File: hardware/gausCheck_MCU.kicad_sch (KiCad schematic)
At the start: 17 parts, among them J2 SWD, SW1 PTS810, U3 ATSAML22N18A-AUT, Y1 32.768kHz

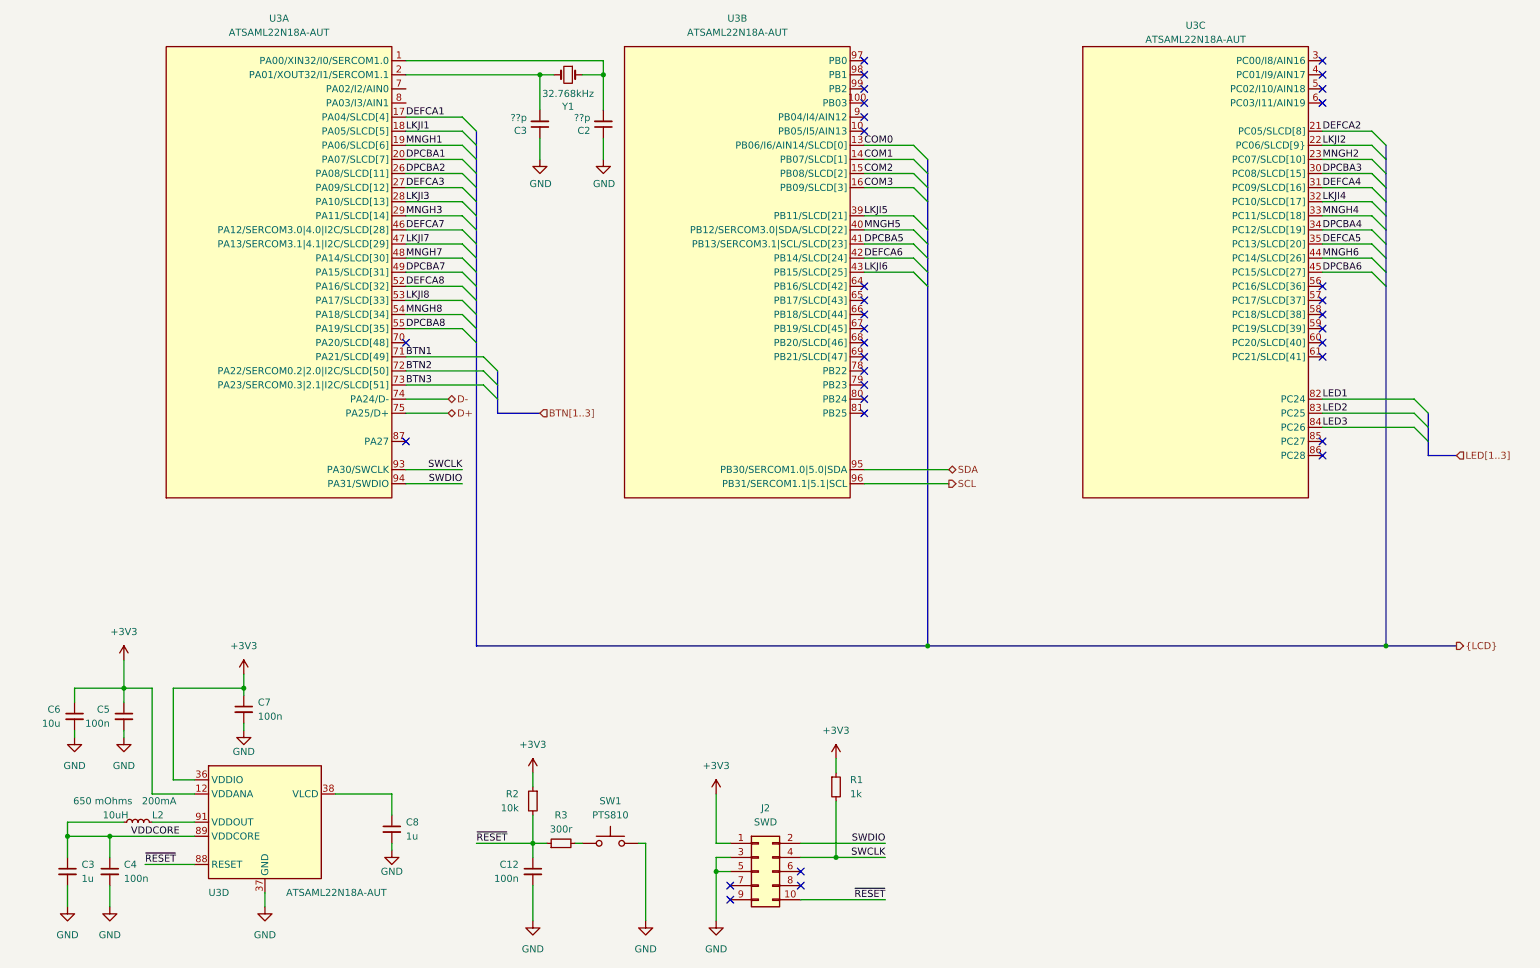
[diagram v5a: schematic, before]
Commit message: moved buttons to the side JTAG to the bottom reset to the bottom
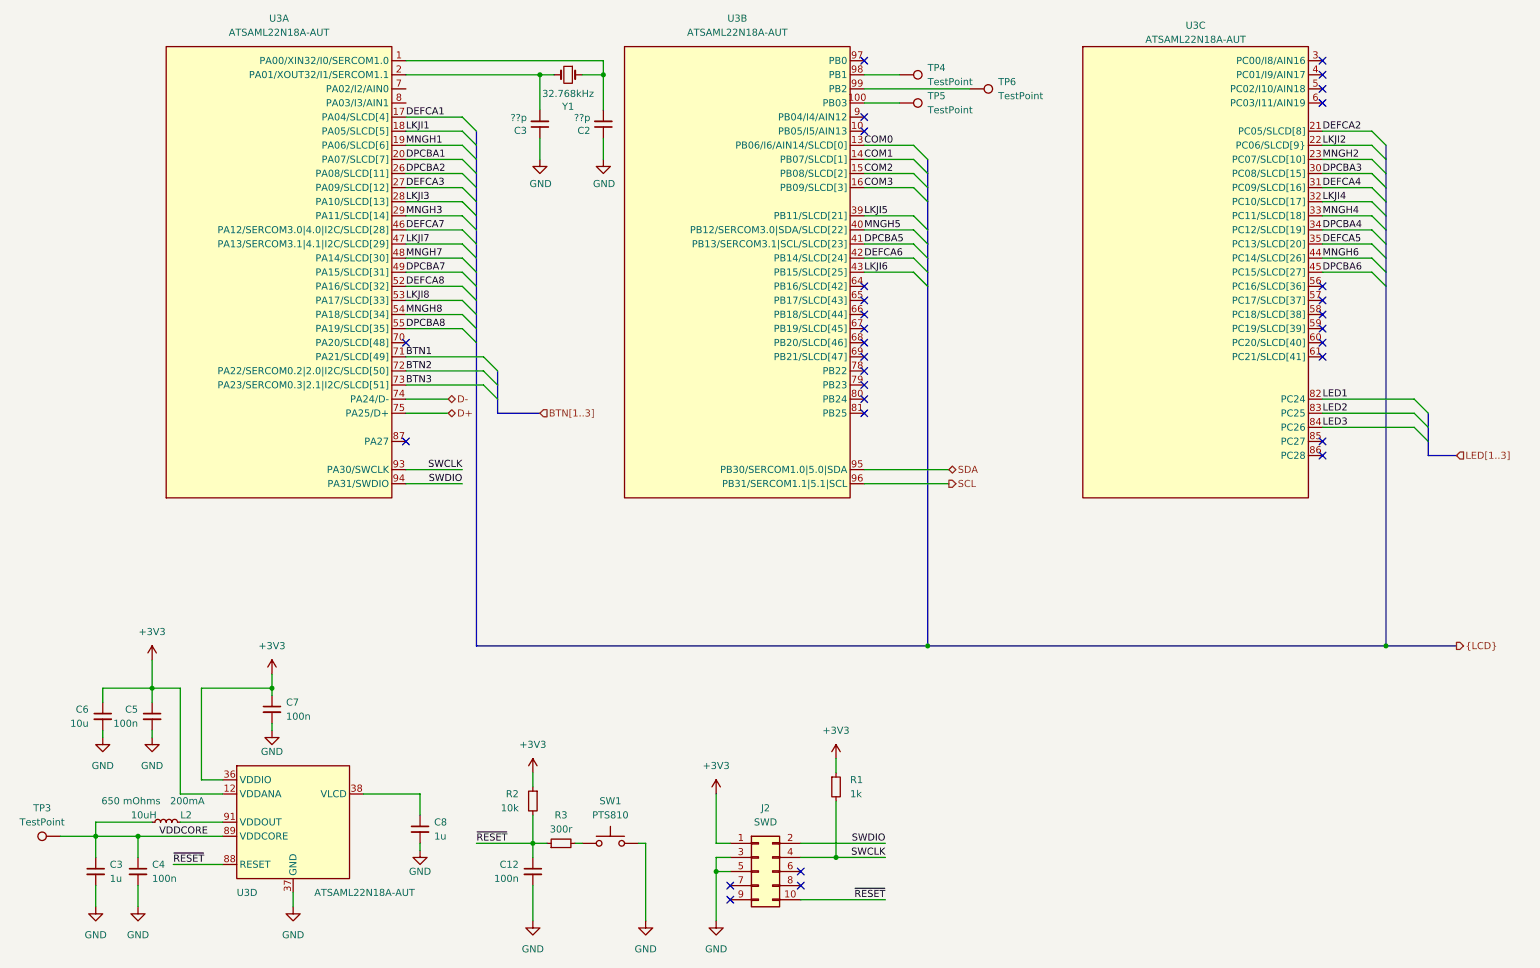
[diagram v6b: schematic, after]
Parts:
- added TP3, TP4, TP5, TP6: TestPoint, TestPoint:TestPoint_Pad_D1.0mm, symbol Connector:TestPoint
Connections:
- net VDDCORE: now also TP3.1
- net at U3.100 (PB03): now also TP5.1
- net at U3.98 (PB1): now also TP4.1
- net at U3.99 (PB2): now also TP6.1
- no-connect marks 34 -> 31
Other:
- moved on the sheet: C3, C4, C5, C6, C7, C8, L2, U3D

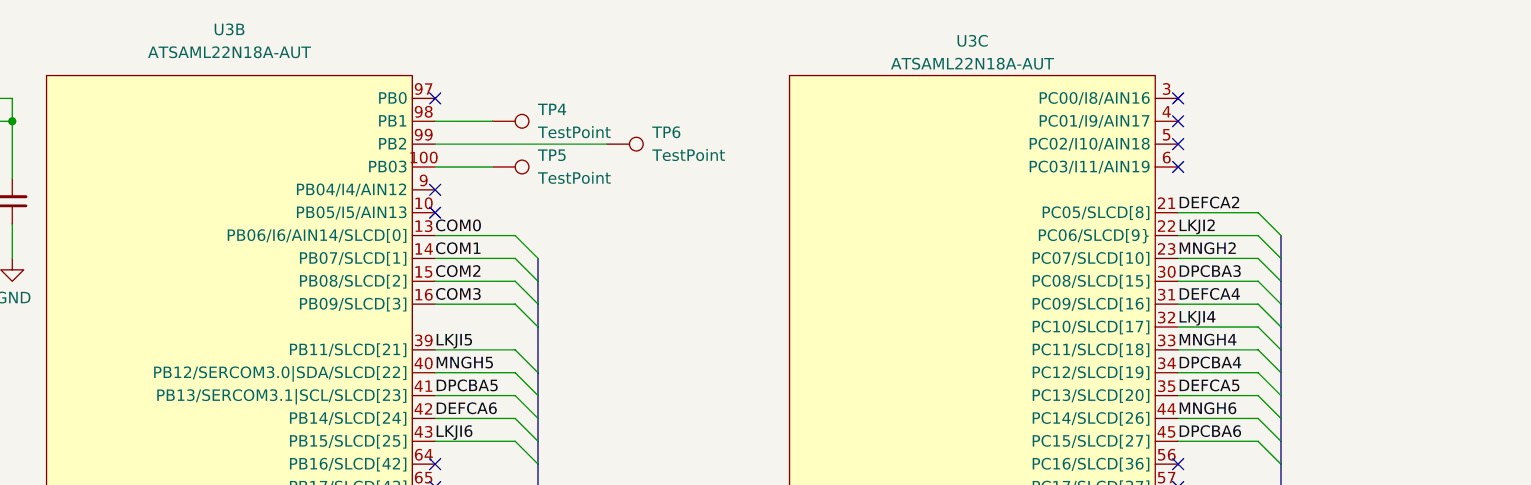
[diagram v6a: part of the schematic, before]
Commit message: added 3V3 LDO added VBat Measurement
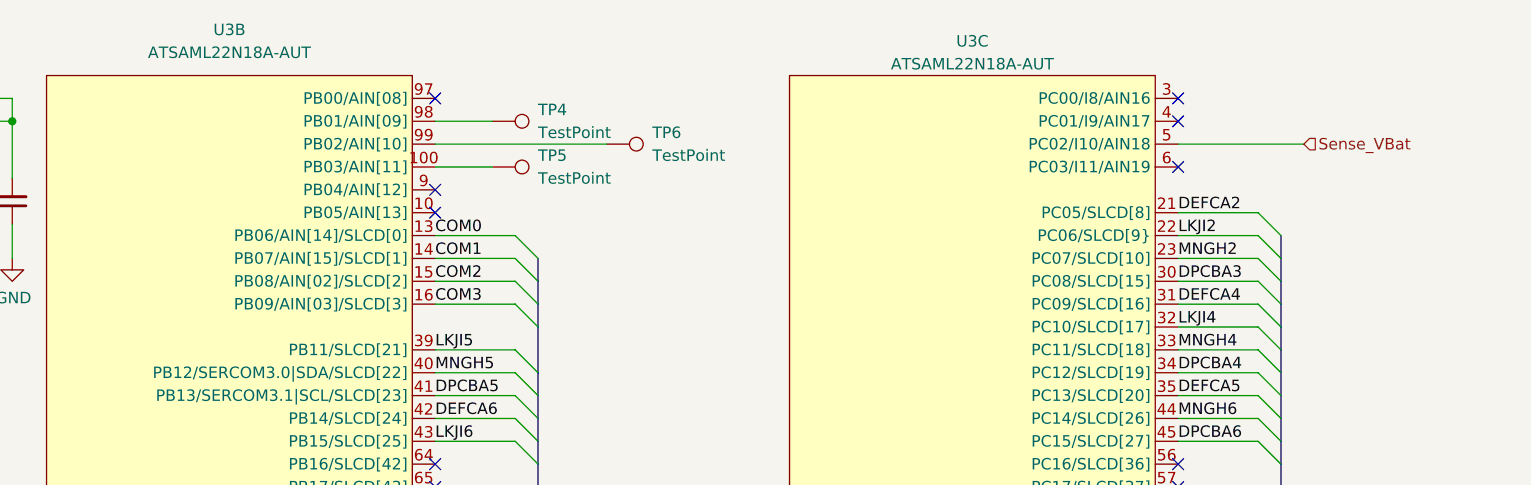
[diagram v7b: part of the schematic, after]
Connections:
- net Sense_VBat: now reaches U3.5 (PC02/I10/AIN18)
- no-connect marks 31 -> 30
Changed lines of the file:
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@@
   (no_connect (at 165.1 93.98))
   (no_connect (at 247.65 73.66))
-  (no_connect (at 247.65 35.56))
   (no_connect (at 247.65 78.74))
   (no_connect (at 82.55 99.06))
@@
     (stroke (width 0) (type default))
   )
+  (wire (pts (xy 247.65 35.56) (xy 261.62 35.56))
+    (stroke (width 0) (type default))
+  )
   (wire (pts (xy 58.42 140.97) (xy 58.42 143.51))
     (stroke (width 0) (type default))
@@
   )
   (hierarchical_label "BTN[1..3]" (shape input) (at 106.68 93.98 0) (fields_autoplaced)
+    (effects (font (size 1.27 1.27)) (justify left))
+  )
+  (hierarchical_label "Sense_VBat" (shape input) (at 261.62 35.56 0) (fields_autoplaced)
     (effects (font (size 1.27 1.27)) (justify left))
   )
@@
     (pin "24")
     (pin "25")
+    (pin "3")
     (instances
       (project "gaussCheck"

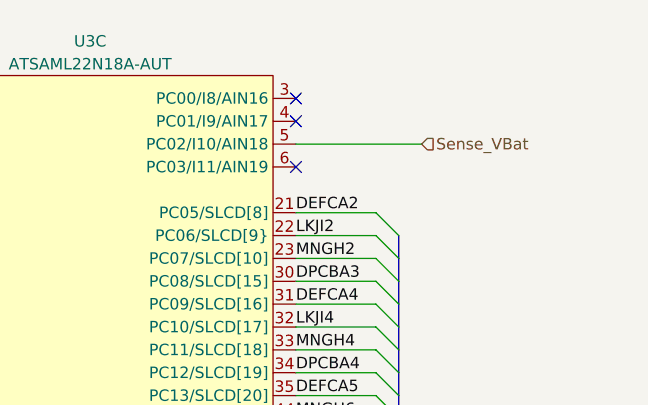
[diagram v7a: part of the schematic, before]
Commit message: added schottky diode to LDO connected en_vbat signal added a drawing of mems axis
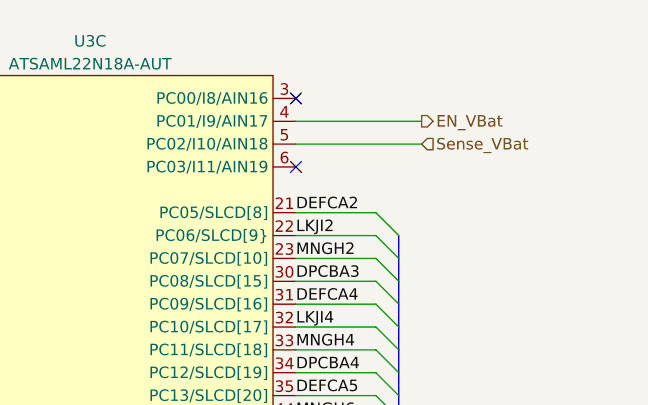
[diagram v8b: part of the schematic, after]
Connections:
- net EN_VBat: now reaches U3.4 (PC01/I9/AIN17)
- no-connect marks 30 -> 29
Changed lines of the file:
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@@
   (no_connect (at 247.65 71.12))
   (no_connect (at 165.1 43.18))
-  (no_connect (at 247.65 33.02))
   (no_connect (at 165.1 91.44))
   (no_connect (at 153.67 176.53))
@@
     (stroke (width 0) (type default))
   )
+  (wire (pts (xy 247.65 33.02) (xy 261.62 33.02))
+    (stroke (width 0) (type default))
+  )
   (wire (pts (xy 45.72 143.51) (xy 45.72 160.02))
     (stroke (width 0) (type default))
@@
     (effects (font (size 1.27 1.27)) (justify left))
   )
+  (hierarchical_label "EN_VBat" (shape output) (at 261.62 33.02 0) (fields_autoplaced)
+    (effects (font (size 1.27 1.27)) (justify left))
+  )
